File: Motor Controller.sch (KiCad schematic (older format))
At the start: 23 parts, among them U10 2X3Header, U13 Motor_mount, U2 DRV8833, U27 Test_Point, U28 Test_Point, U29 Test_Point, U30 Test_Point, U32 Motor_mount, U9 2X3Header

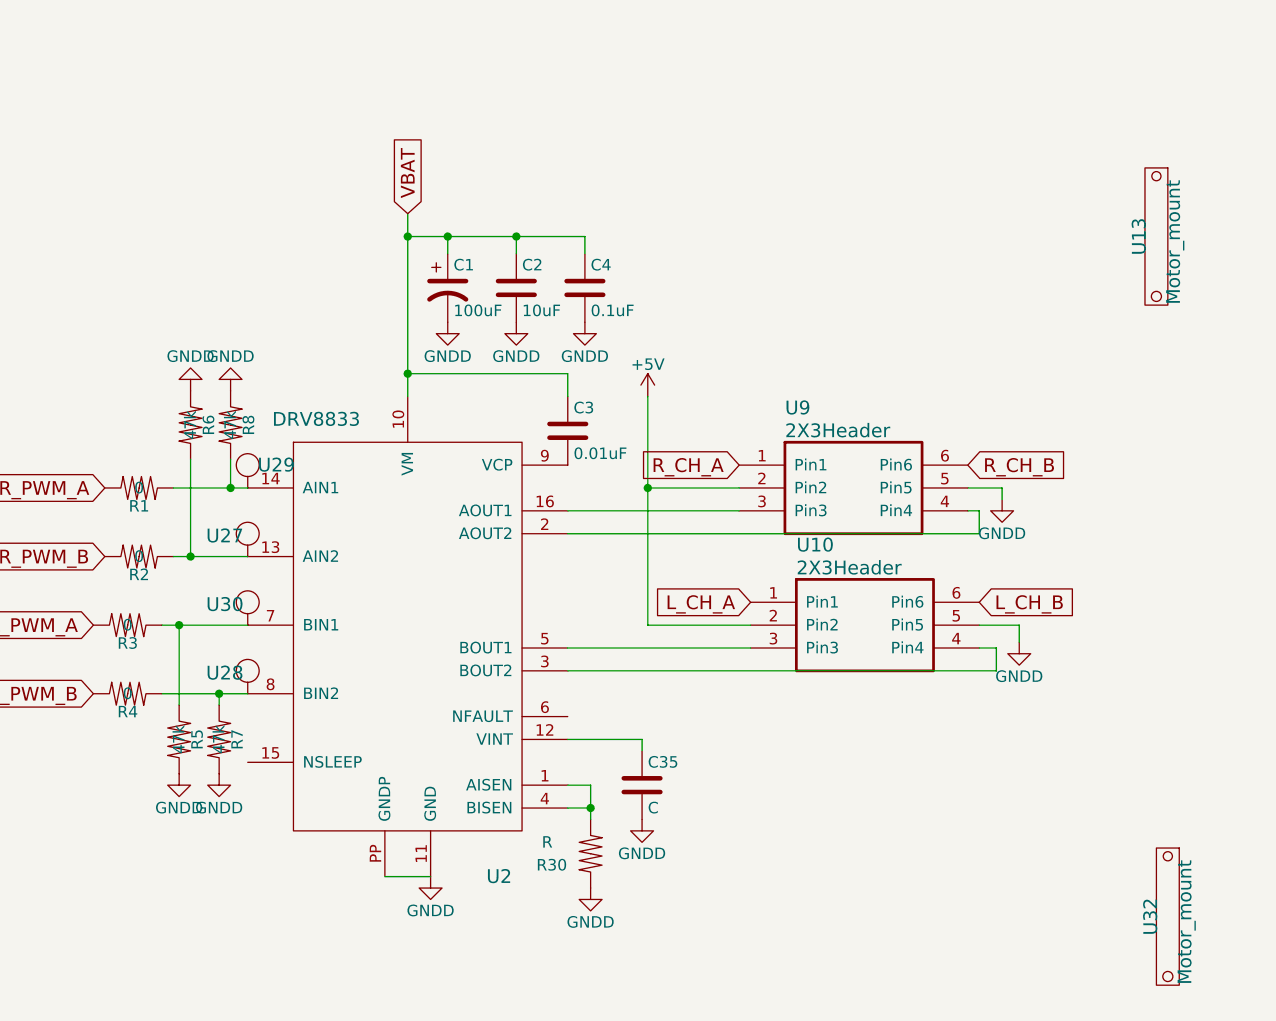
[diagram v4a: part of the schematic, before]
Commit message: made 3D wheel and Tire setup
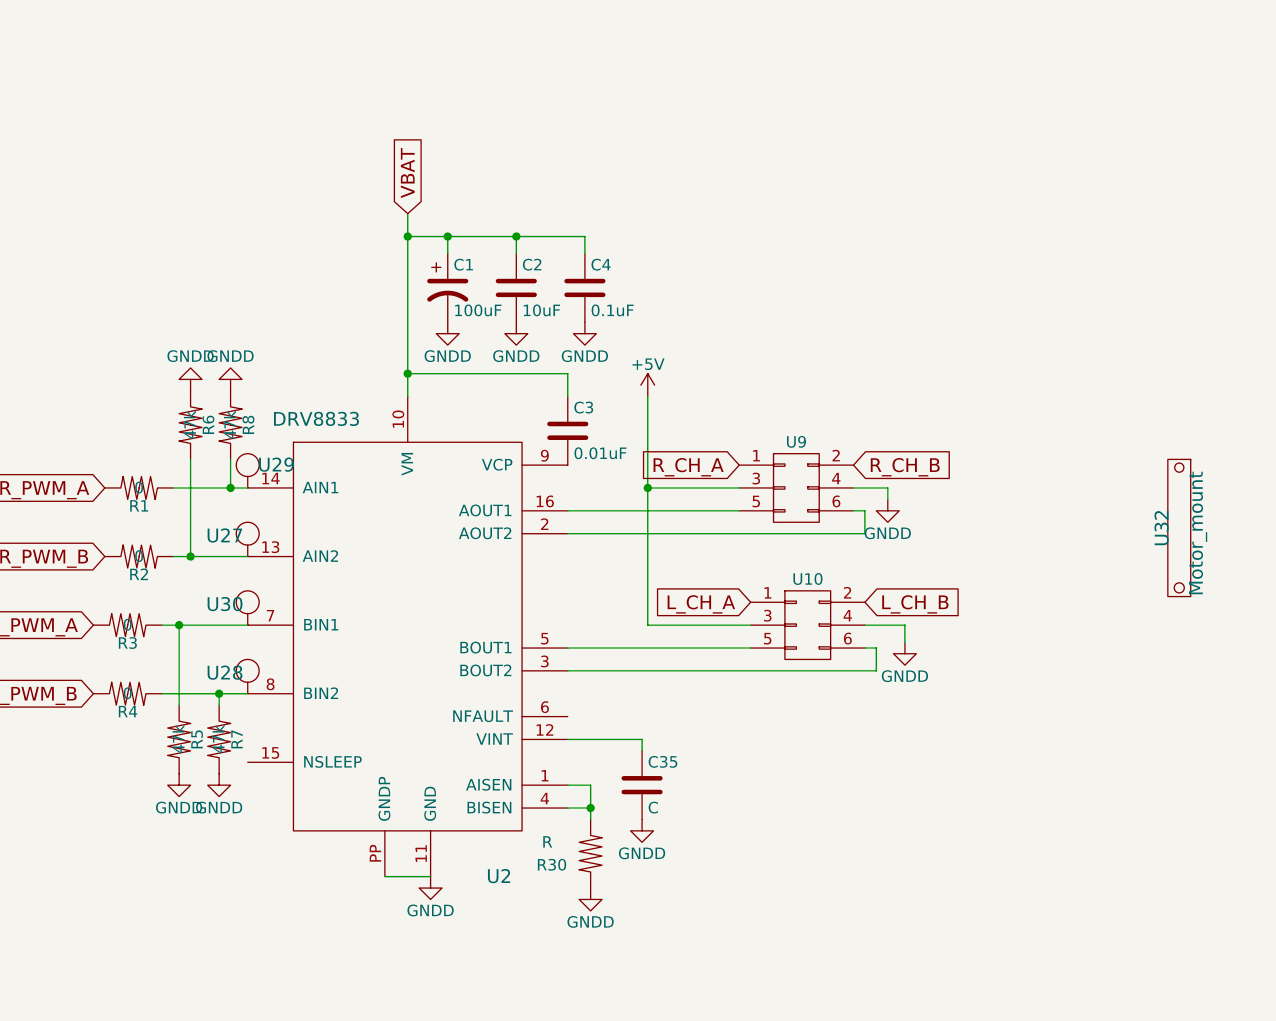
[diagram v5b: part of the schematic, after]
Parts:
- removed U10, U9: 2X3Header, micromouse:Motors_connectors, symbol 2X3Header
- removed U13: Motor_mount, micromouse:Motor_mount, symbol Motor_mount
- added U10, U9: CONN_02X03, symbol CONN_02X03
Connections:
- net +5V: now also U10.3 (P3), U9.3 (P3)
- net GNDD: now also U10.4 (P4), U9.4 (P4)
- net L_CH_A: now also U10.1 (P1)
- net L_CH_B: now also U10.2 (P2)
- net R_CH_A: now also U9.1 (P1)
- net R_CH_B: now also U9.2 (P2)
- net at U2.16 (AOUT1): now also U9.5 (P5)
- net at U2.2 (AOUT2): now also U9.6 (P6)
- net at U2.5 (BOUT1): now also U10.5 (P5)
- net at U2.3 (BOUT2): now also U10.6 (P6)
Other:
- moved on the sheet: U32
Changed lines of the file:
@@
 Comment4 ""
 $EndDescr
-$Comp
-L 2X3Header U9
-U 1 1 5945E464
-P 7350 3275
-F 0 "U9" H 7550 3525 60  0000 L CNN
-F 1 "2X3Header" H 7550 3425 60  0000 L CNN
-F 2 "micromouse:Motors_connectors" H 7350 3275 60  0001 C CNN
-F 3 "" H 7350 3275 60  0001 C CNN
-F 4 "M20-9980345" H 7350 3275 60  0001 C CNN "manf#"
-	1    7350 3275
-	1    0    0    -1
-$EndComp
 Text GLabel 4575 3675 0    60   Input ~ 0
 R_PWM_B
@@
 Text GLabel 7350 3275 0    60   Input ~ 0
 R_CH_A
-Text GLabel 8350 3275 2    60   Input ~ 0
+Text GLabel 7850 3275 2    60   Input ~ 0
 R_CH_B
 $Comp
 L GNDD #PWR01
 U 1 1 5945ED1F
-P 8500 3425
-F 0 "#PWR01" H 8500 3175 50  0001 C CNN
-F 1 "GNDD" H 8500 3275 50  0000 C CNN
-F 2 "" H 8500 3425 50  0001 C CNN
-F 3 "" H 8500 3425 50  0001 C CNN
-	1    8500 3425
+P 8000 3425
+F 0 "#PWR01" H 8000 3175 50  0001 C CNN
+F 1 "GNDD" H 8000 3275 50  0000 C CNN
+F 2 "" H 8000 3425 50  0001 C CNN
+F 3 "" H 8000 3425 50  0001 C CNN
+	1    8000 3425
 	1    0    0    -1
 $EndComp
@@
 $EndComp
 $Comp
-L 2X3Header U10
-U 1 1 5945EF7C
-P 7400 3875
-F 0 "U10" H 7600 4125 60  0000 L CNN
-F 1 "2X3Header" H 7600 4025 60  0000 L CNN
-F 2 "micromouse:Motors_connectors" H 7400 3875 60  0001 C CNN
-F 3 "" H 7400 3875 60  0001 C CNN
-F 4 "M20-9980345" H 7400 3875 60  0001 C CNN "manf#"
-	1    7400 3875
-	1    0    0    -1
-$EndComp
-$Comp
 L R R8
 U 1 1 5945EF88
@@
 Text GLabel 7400 3875 0    60   Input ~ 0
 L_CH_A
-Text GLabel 8400 3875 2    60   Input ~ 0
+Text GLabel 7900 3875 2    60   Input ~ 0
 L_CH_B
 $Comp
 L GNDD #PWR03
 U 1 1 5945EFE1
-P 8575 4050
-F 0 "#PWR03" H 8575 3800 50  0001 C CNN
-F 1 "GNDD" H 8575 3900 50  0000 C CNN
-F 2 "" H 8575 4050 50  0001 C CNN
-F 3 "" H 8575 4050 50  0001 C CNN
-	1    8575 4050
+P 8075 4050
+F 0 "#PWR03" H 8075 3800 50  0001 C CNN
+F 1 "GNDD" H 8075 3900 50  0000 C CNN
+F 2 "" H 8075 4050 50  0001 C CNN
+F 3 "" H 8075 4050 50  0001 C CNN
+	1    8075 4050
 	1    0    0    -1
 $EndComp
@@
 EndData
 $EndBitmap
-Wire Wire Line
-	7350 3375 6950 3375
-Wire Wire Line
-	6950 2975 6950 3975
 $Comp
 L R R4
@@
 L Motor_mount U32
 U 1 1 59B51BD5
-P 9225 5250
-F 0 "U32" H 9225 5175 60  0000 C CNN
-F 1 "Motor_mount" H 9250 5325 60  0000 C CNN
-F 2 "micromouse:Motor_mount" H 9225 5250 60  0001 C CNN
-F 3 "" H 9225 5250 60  0001 C CNN
-	1    9225 5250
-	0    1    1    0
-$EndComp
-$Comp
-L Motor_mount U13
-U 1 1 59B51CD6
-P 9175 2275
-F 0 "U13" H 9175 2200 60  0000 C CNN
-F 1 "Motor_mount" H 9200 2350 60  0000 C CNN
-F 2 "micromouse:Motor_mount" H 9175 2275 60  0001 C CNN
-F 3 "" H 9175 2275 60  0001 C CNN
-	1    9175 2275
+P 9275 3550
+F 0 "U32" H 9275 3475 60  0000 C CNN
+F 1 "Motor_mount" H 9300 3625 60  0000 C CNN
+F 2 "micromouse:Motor_mount" H 9275 3550 60  0001 C CNN
+F 3 "" H 9275 3550 60  0001 C CNN
+	1    9275 3550
 	0    1    1    0
 $EndComp
@@
 	1    0    0    -1
 $EndComp
-Wire Wire Line
-	6600 3475 7350 3475
-Wire Wire Line
-	8350 3475 8400 3475
-Wire Wire Line
-	8400 3475 8400 3575
-Wire Wire Line
-	8400 3575 6600 3575
-Wire Wire Line
-	8350 3375 8500 3375
-Wire Wire Line
-	8500 3375 8500 3425
-Wire Wire Line
-	6950 3975 7400 3975
-Connection ~ 6950 3375
-Wire Wire Line
-	6600 4075 7400 4075
-Wire Wire Line
-	6600 4175 8475 4175
-Wire Wire Line
-	8475 4175 8475 4075
-Wire Wire Line
-	8475 4075 8400 4075
-Wire Wire Line
-	8400 3975 8575 3975
-Wire Wire Line
-	8575 3975 8575 4050
 $Comp
 L R R30
@@
 	1    0    0    -1
 $EndComp
-Wire Wire Line
-	6600 4675 6700 4675
-Wire Wire Line
-	6700 4675 6700 4825
-Wire Wire Line
-	6600 4775 6700 4775
-Connection ~ 6700 4775
 $Comp
 L GNDD #PWR04
@@
 	1    0    0    -1
 $EndComp
-Wire Wire Line
-	5800 5075 6000 5075
 $Comp
 L C C35
@@
 	1    0    0    -1
 $EndComp
-Wire Wire Line
-	6600 4475 6925 4475
-Wire Wire Line
-	6925 4475 6925 4525
 $Comp
 L GNDD #PWR06
@@
 	1    0    0    -1
 $EndComp
-Wire Wire Line
-	6600 2975 6600 2875
-Wire Wire Line
-	6600 2875 5900 2875
-Wire Wire Line
-	5900 2175 5900 2975
 $Comp
 L GNDD #PWR07
@@
 	1    0    0    -1
 $EndComp
-Wire Wire Line
-	5900 2275 6675 2275
-Wire Wire Line
-	6675 2275 6675 2350
-Connection ~ 5900 2875
-Wire Wire Line
-	6375 2350 6375 2275
-Connection ~ 6375 2275
-Wire Wire Line
-	6075 2350 6075 2275
-Connection ~ 6075 2275
-Connection ~ 5900 2275
 $Comp
 L CP1 C1
@@
 	1    0    0    -1
 $EndComp
-Wire Wire Line
-	4875 3375 5200 3375
-Wire Wire Line
-	4950 3250 4950 3675
-Wire Wire Line
-	4875 3675 5200 3675
-Connection ~ 4950 3675
-Wire Wire Line
-	5125 3250 5125 3375
-Connection ~ 5125 3375
-Wire Wire Line
-	5200 3975 4825 3975
-Wire Wire Line
-	5200 4275 4825 4275
-Wire Wire Line
-	4900 4325 4900 3975
-Connection ~ 4900 3975
-Wire Wire Line
-	5075 4325 5075 4275
-Connection ~ 5075 4275
 $Comp
 L GNDD #PWR010
@@
 	-1   0    0    1
 $EndComp
+$Comp
+L CONN_02X03 U9
+U 1 1 59CA1E36
+P 7600 3375
+F 0 "U9" H 7600 3575 50  0000 C CNN
+F 1 "CONN_02X03" H 7600 3175 50  0001 C CNN
+F 2 "" H 7600 2175 50  0001 C CNN
+F 3 "" H 7600 2175 50  0001 C CNN
+	1    7600 3375
+	1    0    0    -1
+$EndComp
+$Comp
+L CONN_02X03 U10
+U 1 1 59CA224A
+P 7650 3975
+F 0 "U10" H 7650 4175 50  0000 C CNN
+F 1 "CONN_02X03" H 7650 3775 50  0001 C CNN
+F 2 "" H 7650 2775 50  0001 C CNN
+F 3 "" H 7650 2775 50  0001 C CNN
+	1    7650 3975
+	1    0    0    -1
+$EndComp
+Wire Wire Line
+	7950 4075 7900 4075
+Wire Wire Line
+	7950 4175 7950 4075
+Wire Wire Line
+	6600 4175 7950 4175
+Wire Wire Line
+	7900 3475 7850 3475
+Wire Wire Line
+	7900 3575 7900 3475
+Wire Wire Line
+	6600 3575 7900 3575
+Connection ~ 5075 4275
+Wire Wire Line
+	5075 4325 5075 4275
+Connection ~ 4900 3975
+Wire Wire Line
+	4900 4325 4900 3975
+Wire Wire Line
+	4825 4275 5200 4275
+Wire Wire Line
+	4825 3975 5200 3975
+Connection ~ 5125 3375
+Wire Wire Line
+	5125 3250 5125 3375
+Connection ~ 4950 3675
+Wire Wire Line
+	4875 3675 5200 3675
+Wire Wire Line
+	4950 3250 4950 3675
+Wire Wire Line
+	4875 3375 5200 3375
+Connection ~ 5900 2275
+Connection ~ 6075 2275
+Wire Wire Line
+	6075 2350 6075 2275
+Connection ~ 6375 2275
+Wire Wire Line
+	6375 2350 6375 2275
+Connection ~ 5900 2875
+Wire Wire Line
+	6675 2275 6675 2350
+Wire Wire Line
+	5900 2275 6675 2275
+Wire Wire Line
+	5900 2175 5900 2975
+Wire Wire Line
+	6600 2875 5900 2875
+Wire Wire Line
+	6600 2975 6600 2875
+Wire Wire Line
+	6925 4475 6925 4525
+Wire Wire Line
+	6600 4475 6925 4475
+Wire Wire Line
+	5800 5075 6000 5075
+Connection ~ 6700 4775
+Wire Wire Line
+	6600 4775 6700 4775
+Wire Wire Line
+	6700 4675 6700 4825
+Wire Wire Line
+	6600 4675 6700 4675
+Wire Wire Line
+	8075 3975 8075 4050
+Wire Wire Line
+	7900 3975 8075 3975
+Wire Wire Line
+	6600 4075 7400 4075
+Connection ~ 6950 3375
+Wire Wire Line
+	6950 3975 7400 3975
+Wire Wire Line
+	8000 3375 8000 3425
+Wire Wire Line
+	7850 3375 8000 3375
+Wire Wire Line
+	6600 3475 7350 3475
+Wire Wire Line
+	6950 2975 6950 3975
+Wire Wire Line
+	7350 3375 6950 3375
 $EndSCHEMATC

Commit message: changed the MCU to MK20DX256VLH7
-changed the MCU to MK20DX256VLH7
-This branch is deprciated as I am changing back to the K66 series MCU
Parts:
- C1, C3: footprint (none) -> Capacitors_SMD:C_0603
- R30: footprint (none) -> micromouse:C_0603
- U10, U9: footprint (none) -> micromouse:Motor_Connector
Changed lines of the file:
@@
 F 0 "R30" H 6530 4925 50  0000 C CNN
 F 1 "R" H 6510 5025 50  0000 C CNN
-F 2 "" H 6700 4975 60  0001 C CNN
+F 2 "micromouse:C_0603" H 6700 4975 60  0001 C CNN
 F 3 "" H 6700 4975 60  0001 C CNN
 	1    6700 4975
@@
 F 0 "C3" H 6625 3225 50  0000 L CNN
 F 1 "0.01uF" H 6625 3025 50  0000 L CNN
-F 2 "" H 6638 2975 50  0000 C CNN
+F 2 "Capacitors_SMD:C_0603" H 6638 2975 50  0001 C CNN
 F 3 "" H 6600 3125 50  0000 C CNN
 F 4 "GRM188R71E103KA01D" H 6600 3125 60  0001 C CNN "manf#"
@@
 F 0 "C1" H 6100 2600 50  0000 L CNN
 F 1 "100uF" H 6100 2400 50  0000 L CNN
-F 2 "" H 6075 2500 50  0001 C CNN
+F 2 "Capacitors_SMD:C_0603" H 6075 2500 50  0001 C CNN
 F 3 "" H 6075 2500 50  0001 C CNN
 F 4 "RNE1C101MDS1PX" H 6075 2500 60  0001 C CNN "manf#"
@@
 F 0 "U9" H 7600 3575 50  0000 C CNN
 F 1 "CONN_02X03" H 7600 3175 50  0001 C CNN
-F 2 "" H 7600 2175 50  0001 C CNN
+F 2 "micromouse:Motor_Connector" H 7600 2175 50  0001 C CNN
 F 3 "" H 7600 2175 50  0001 C CNN
 	1    7600 3375
@@
 F 0 "U10" H 7650 4175 50  0000 C CNN
 F 1 "CONN_02X03" H 7650 3775 50  0001 C CNN
-F 2 "" H 7650 2775 50  0001 C CNN
+F 2 "micromouse:Motor_Connector" H 7650 2775 50  0001 C CNN
 F 3 "" H 7650 2775 50  0001 C CNN
 	1    7650 3975
